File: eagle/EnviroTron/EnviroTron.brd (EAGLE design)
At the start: 27.9 x 39.4 mm, 14 parts

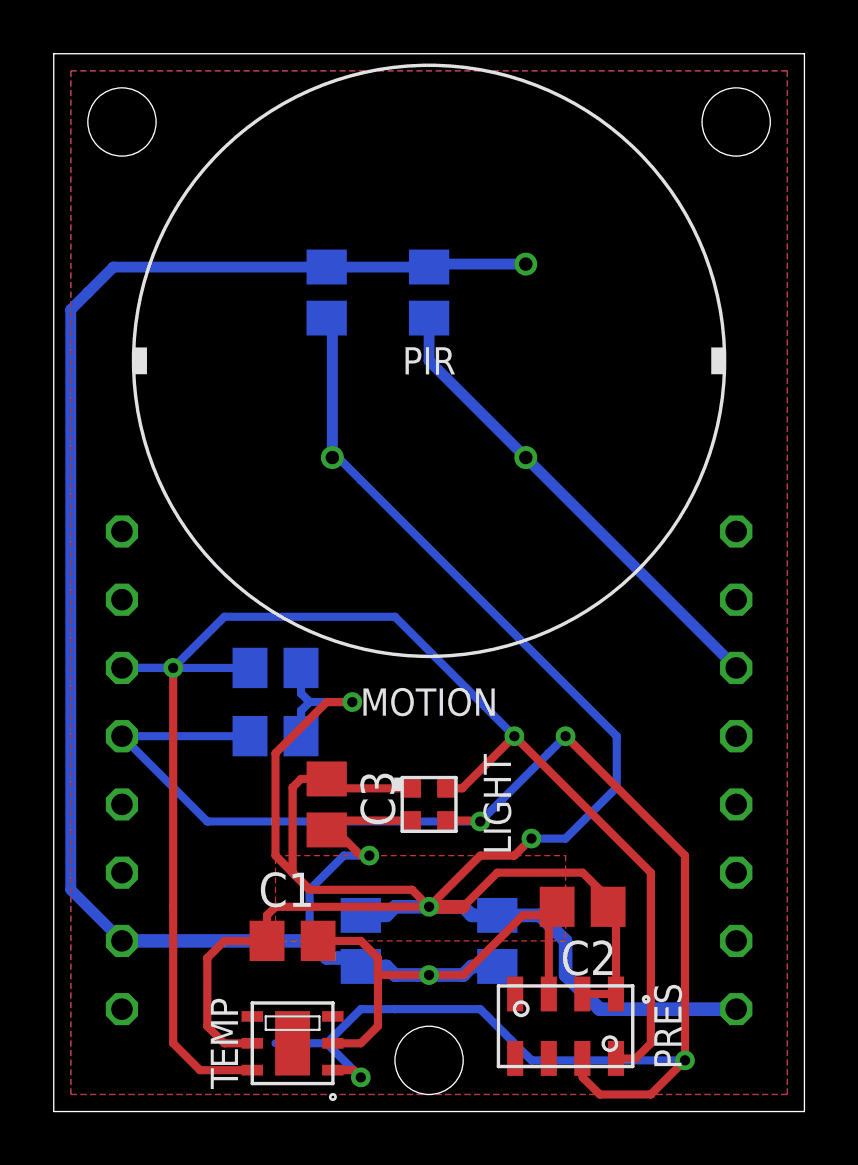
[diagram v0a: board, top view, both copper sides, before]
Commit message: Cleaned up small layout details
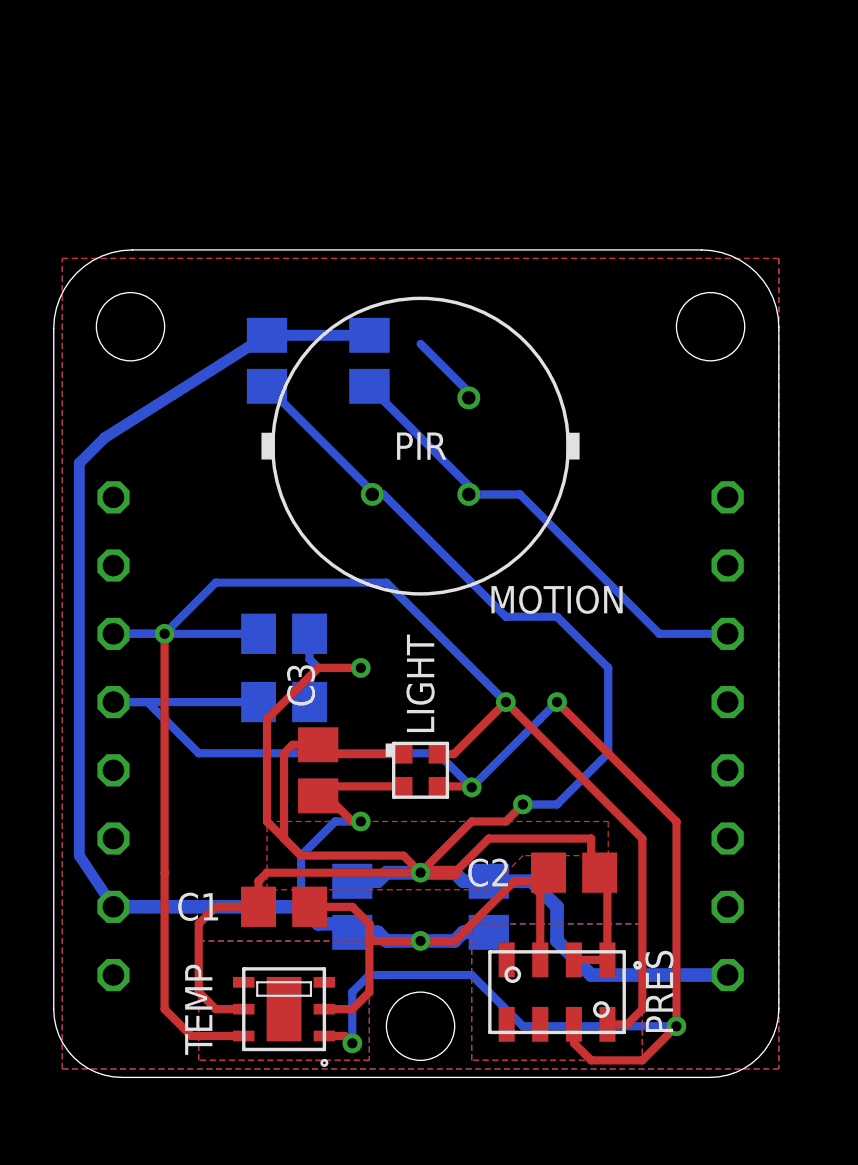
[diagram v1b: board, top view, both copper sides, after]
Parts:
- removed U$2: WEMOS-D1-MINI, Enviro:WEMOS-D1-MINI
- added COMMS: WEMOS-D1-MINI, EnviroTron:WEMOS-D1-MINI
- LIGHT: device Enviro:CHIPLED4 -> EnviroTron:CHIPLED4
- MOTION: device Enviro:CAN3 -> EnviroTron:CAN3
- PRES: device Enviro:DFN8 -> EnviroTron:DFN8
- TEMP: device Enviro:SHT2X-DFN6 -> EnviroTron:SHT2X-DFN6
- moved C4 3.38 mm to (7.94, 26.7)
- moved R3 3.38 mm to (11.7, 26.7)
- moved MOTION 3.19 mm to (13.7, 23.5)
- moved R1 1.31 mm to (8.57, 16.5)
- moved R2 1.31 mm to (8.57, 14.0)
- moved C2 1.31 mm to (19.4, 7.62)
- moved C6 1.31 mm to (16.2, 6.35)
- moved C1 1.31 mm to (8.57, 6.35)
- moved C3 1.31 mm to (9.84, 11.4)
- moved LIGHT 1.31 mm to (13.7, 11.4)
- moved TEMP 1.31 mm to (8.57, 2.54)
- moved PRES 1.31 mm to (18.7, 3.17)
- moved C5 1.31 mm to (11.1, 6.35)
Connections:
- net 3V3: now also COMMS.3V3; no longer U$2.3V3
- net GND: now also COMMS.GND; no longer U$2.GND
- net PIROUT: now also COMMS.D0; no longer U$2.D0
- net SCL: now also COMMS.D1; no longer U$2.D1
- net SDA: now also COMMS.D2; no longer U$2.D2
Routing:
- net GND: track 85.6 -> 75.6 mm
- net SDA: track 63.9 -> 61.2 mm
- net 3V3: track 101.0 -> 100.2 mm
- net SCL: track 57.7 -> 58.3 mm
- added copper zone on layer 1, net N$1
- added copper zone on layer 16, net N$1
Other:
- board size 27.9 x 39.4 mm -> 27 x 30.8 mm

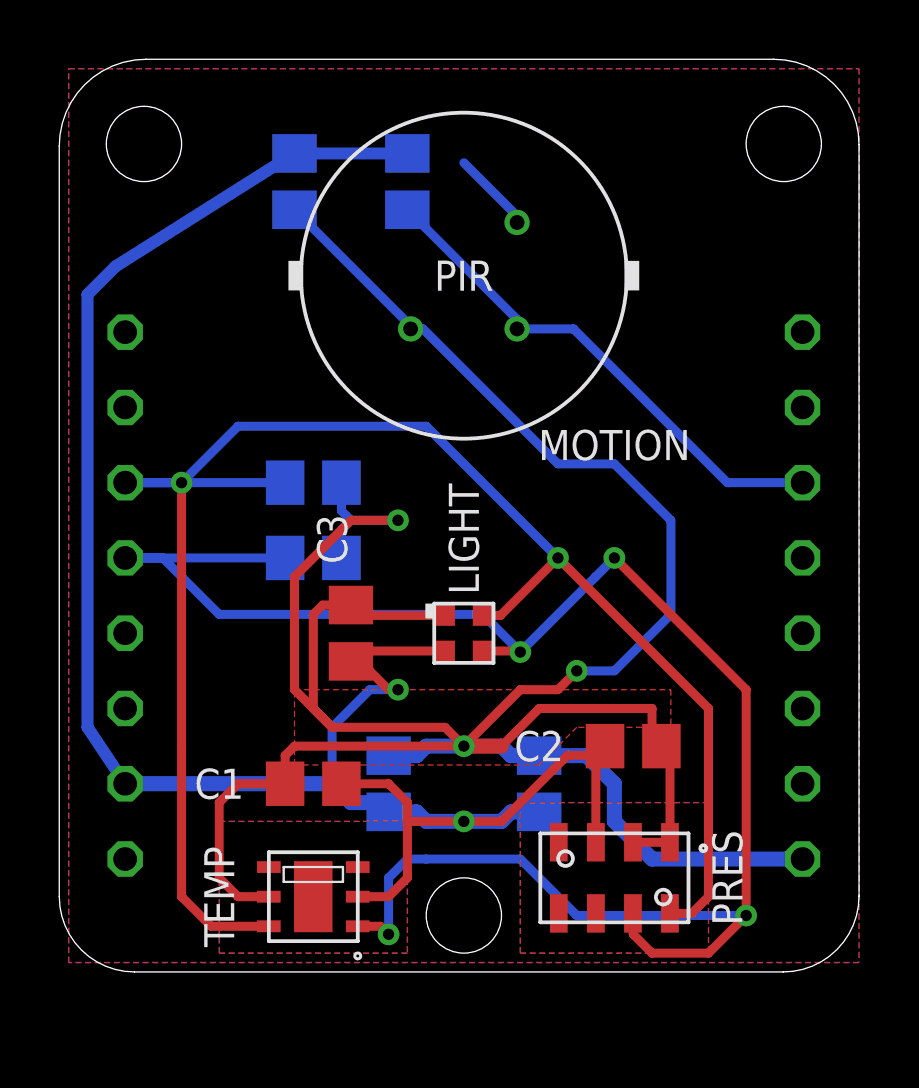
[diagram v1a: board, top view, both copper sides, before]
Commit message: Fixed floating CSB pin on MS5607 chip
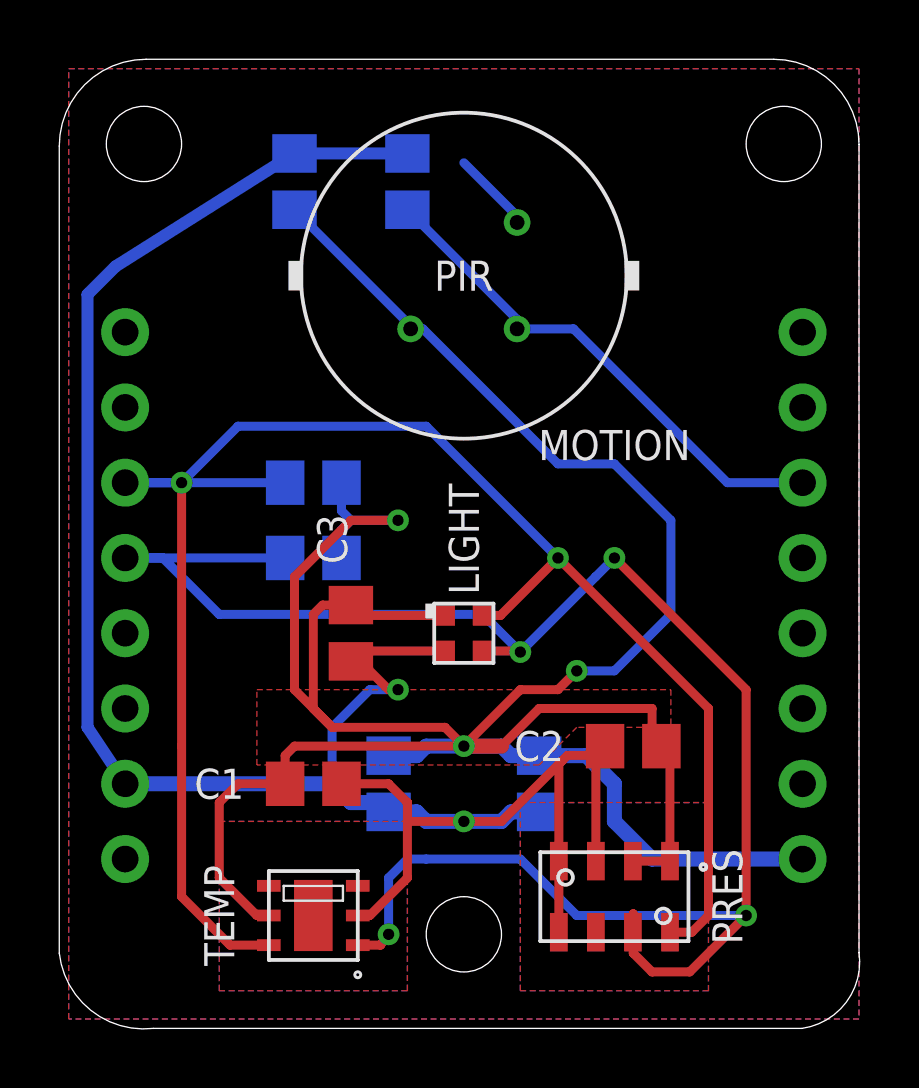
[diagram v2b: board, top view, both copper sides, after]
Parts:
- moved TEMP 0.64 mm to (8.57, 1.91)
- moved PRES 0.63 mm to (18.7, 2.54)
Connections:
- net GND: now also PRES.4, PRES.5
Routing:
- net GND: track 75.6 -> 82.4 mm
- net SDA: track 61.2 -> 62.8 mm
- net 3V3: track 100.2 -> 101.1 mm
- net SCL: track 58.3 -> 59.2 mm
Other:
- board size 27 x 30.8 mm -> 27 x 32.7 mm

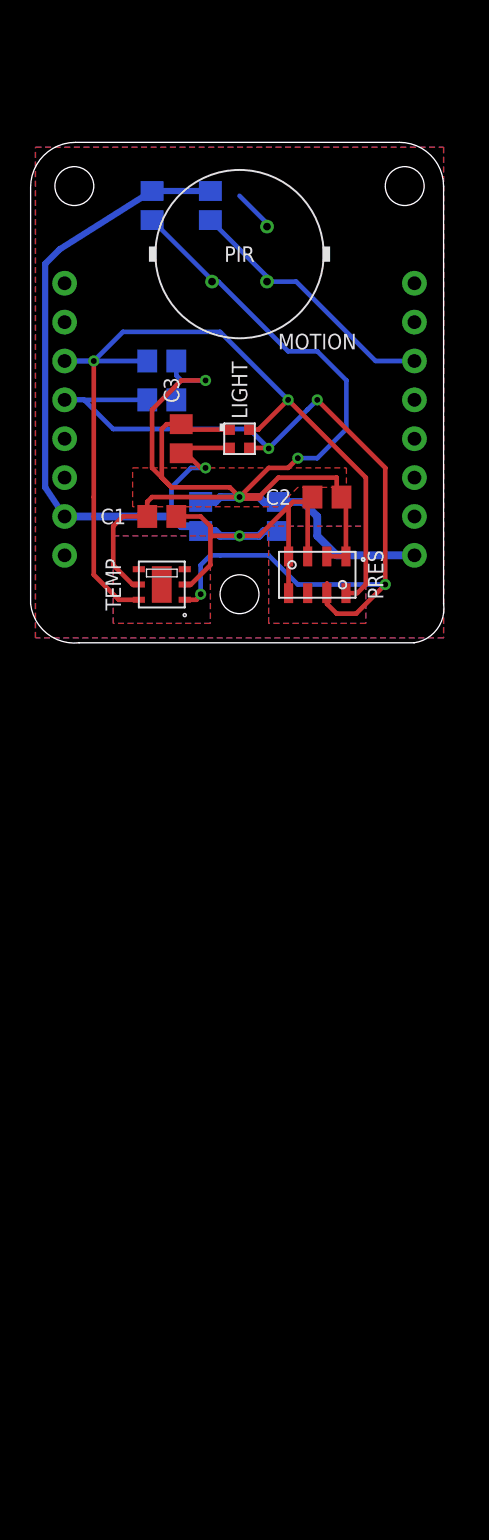
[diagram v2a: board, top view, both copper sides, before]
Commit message: Added sound sensor to EnviroTron board. Swapped to better Pressure sensor.
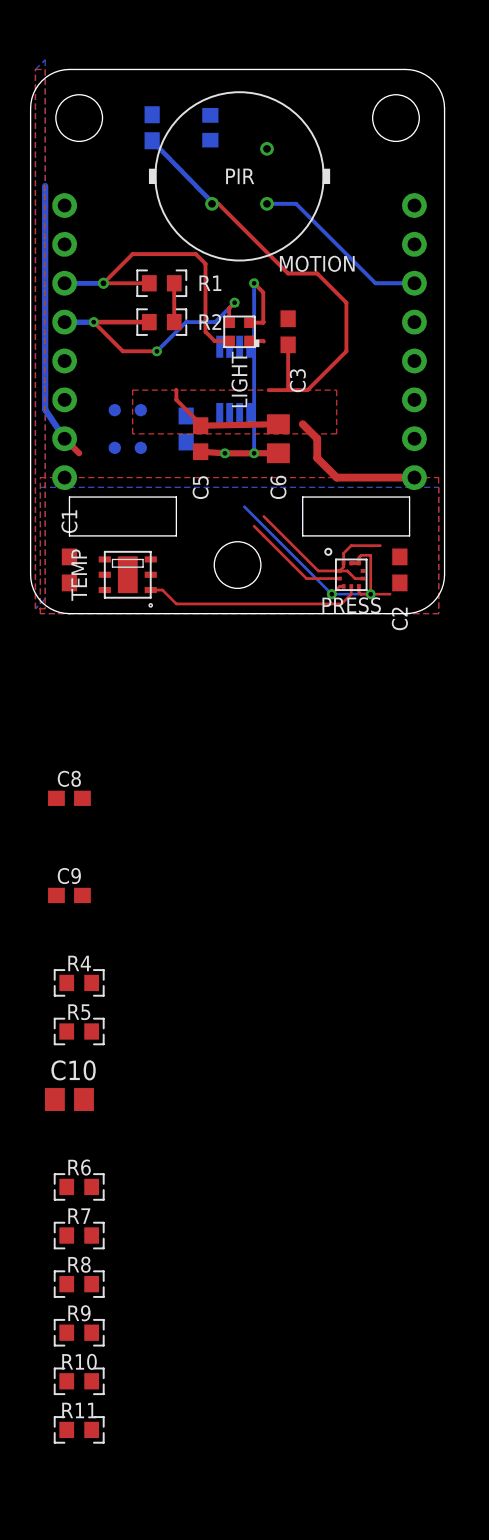
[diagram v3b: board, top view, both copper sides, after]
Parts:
- removed PRES: MS5607, EnviroTron:DFN8
- added C10: 10u, rcl:C0805
- added C7: 100n, SmslsTron-1:C0603
- added C8, C9: 1u, SmslsTron-1:C0603
- added PRESS: LPS22HB, EnviroTron:HLGA-10L
- added R10, R8: 300k, SmslsTron-1:R0603
- added R11, R5, R9: 10k, SmslsTron-1:R0603
- added R4: 2.2k, SmslsTron-1:R0603
- added R6, R7: 1M, SmslsTron-1:R0603
- added SOUND: SPU0410HR5H, EnviroTron:BPAD-4
- added U$1: MCP6002, EnviroTron:MSOP-8
- C1, C2, C3, C4, C5: device rcl:C0805 -> SmslsTron-1:C0603
- R1, R2, R3: device rcl:R0805 -> SmslsTron-1:R0603
- moved C3 9.88 mm to (16.8, 18.4), turned to 90 degrees
- moved LIGHT 6.98 mm to (13.7, 18.4), turned to 90 degrees
- moved C1 6.97 mm to (2.54, 2.86), turned to 270 degrees
- moved C2 6.74 mm to (24.1, 2.86), turned to 270 degrees
- moved COMMS 5.08 mm to (13.7, 17.8)
- moved C5 5.08 mm to (11.1, 11.4), flipped to the top
- moved C6 5.08 mm to (16.2, 11.4), flipped to the top
- moved R2 5.08 mm to (8.57, 19.1), flipped to the top, turned to 0 degrees
- moved C4 5.08 mm to (7.94, 31.8)
- moved MOTION 5.08 mm to (13.7, 28.6)
- moved R1 5.08 mm to (8.57, 21.6), flipped to the top, turned to 0 degrees
- moved R3 5.08 mm to (11.7, 31.8)
- moved TEMP 2.31 mm to (6.35, 2.54)
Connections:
- new net AMP-OUT: COMMS.A0, R10.1, U$1.7
- new net MIC-OUT: R4.2, R6.2, R7.1, SOUND.4, U$1.3
- new net N$10: C9.1, R11.2
- new net N$11: C8.2, C9.2
- new net N$2: R8.1, U$1.1, U$1.5
- new net N$3: C5.1, C6.1
- new net N$4: C5.2, C6.2
- new net N$5: C10.1, R4.1, R5.2
- new net N$6: R8.2, R9.1, U$1.2
- new net N$7: C8.1, R9.2
- new net N$9: R10.2, R11.1, U$1.6
- net 3V3: now also C7.1, PRESS.1, PRESS.10, PRESS.6, R5.1, R6.1, SOUND.1; no longer C5.1, C6.1, PRES.1, PRES.2
- net GND: now also C10.2, C7.2, PRESS.3, PRESS.5, PRESS.8, PRESS.9, R7.2, SOUND.2, SOUND.3; no longer C5.2, C6.2, PRES.3, PRES.4, PRES.5
- net SCL: now also PRESS.2; no longer PRES.8
- net SDA: now also PRESS.4; no longer PRES.7
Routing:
- net 3V3: track 101.1 -> 56.9 mm, vias 3 -> 0
- net GND: track 82.4 -> 51.4 mm, vias 2 -> 4
- net SCL: track 59.2 -> 29.0 mm, vias 2 -> 1
- net SDA: track 62.8 -> 34.5 mm, vias 4 -> 3
- net PIROUT: track 17.7 -> 12.1 mm
- net N$4: track 0.00 -> 5.09 mm, vias 0 -> 1
- net N$3: track 0.00 -> 5.08 mm
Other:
- board size 27 x 32.7 mm -> 27.1 x 35.6 mm

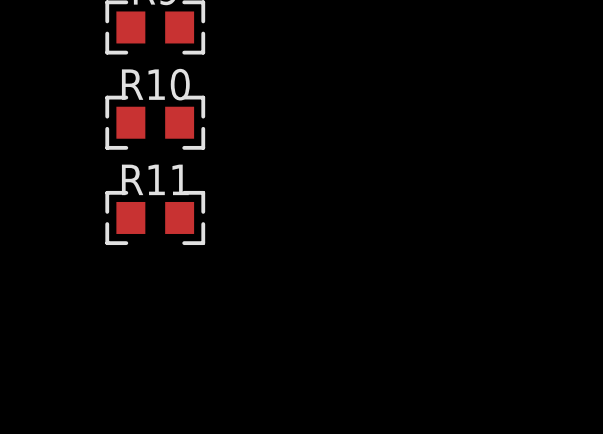
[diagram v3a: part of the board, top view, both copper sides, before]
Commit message: Added DC blocking cap to mic pre-amp circuit.
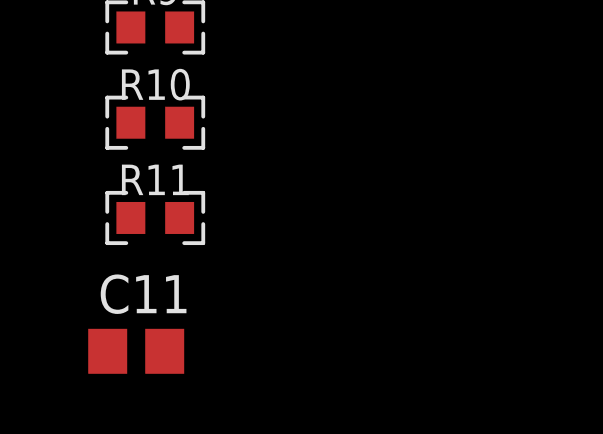
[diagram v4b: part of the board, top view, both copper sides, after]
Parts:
- added C11: 33n, rcl:C0805
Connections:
- new net N$8: C11.1, R4.2, SOUND.4
- net MIC-OUT: now also C11.2; no longer R4.2, SOUND.4
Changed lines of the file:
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@@
 <attribute name="PN-DK" value="" x="3.175" y="-53.34" size="1.778" layer="27" display="off"/>
 </element>
+<element name="C11" library="rcl" package="C0805" value="33n" x="2.54" y="-57.785"/>
 </elements>
 <signals>
@@
 </signal>
 <signal name="MIC-OUT">
-<contactref element="SOUND" pad="4"/>
-<contactref element="R4" pad="2"/>
 <contactref element="R6" pad="2"/>
 <contactref element="R7" pad="1"/>
 <contactref element="U$1" pad="3"/>
+<contactref element="C11" pad="2"/>
+<wire x1="2.3622" y1="-40.64" x2="3.49" y2="-57.785" width="0" layer="19" extent="1-1"/>
 <wire x1="3.9878" y1="-37.465" x2="2.3622" y2="-40.64" width="0" layer="19" extent="1-1"/>
-<wire x1="3.9878" y1="-24.13" x2="3.9878" y2="-37.465" width="0" layer="19" extent="1-1"/>
-<wire x1="7.2" y1="13.295" x2="3.9878" y2="-24.13" width="0" layer="19" extent="1-16"/>
-<wire x1="13.66" y1="17.44" x2="7.2" y2="13.295" width="0" layer="19" extent="16-16"/>
+<wire x1="13.66" y1="17.44" x2="3.9878" y2="-37.465" width="0" layer="19" extent="1-16"/>
 </signal>
 <signal name="N$3">
@@
 <wire x1="3.39" y1="-12.065" x2="3.39" y2="-18.415" width="0" layer="19" extent="1-1"/>
 </signal>
+<signal name="N$8">
+<contactref element="SOUND" pad="4"/>
+<contactref element="R4" pad="2"/>
+<contactref element="C11" pad="1"/>
+<wire x1="3.9878" y1="-24.13" x2="1.59" y2="-57.785" width="0" layer="19" extent="1-1"/>
+<wire x1="7.2" y1="13.295" x2="3.9878" y2="-24.13" width="0" layer="19" extent="1-16"/>
+</signal>
 </signals>
